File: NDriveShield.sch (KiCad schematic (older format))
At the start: 47 parts, among them J1 M03, J2 M03, J3 M03, J4 M03, J5 M03, J6 M03, Q1 NTD5867NLT4G, Q2 NTD5867NLT4G, Q3 NTD5867NLT4G, Q4 NTD5867NLT4G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

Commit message: Draft layout 1
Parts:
- removed J6: M03, symbol M03
- removed Q6: NTD5867NLT4G, symbol MOSFET_N
- removed RG6: 1K, symbol RES
- removed RG7: 10K, symbol RES
- removed SJD1, SJD2, SJD3, SJD4, SJD5, SJD6, SJG6, SJS6: SJ, symbol SJ
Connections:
- net labels removed: D11, DRAIN6, GATE6, SOURCE6, VCC, VIN
- wire segments 113 -> 95

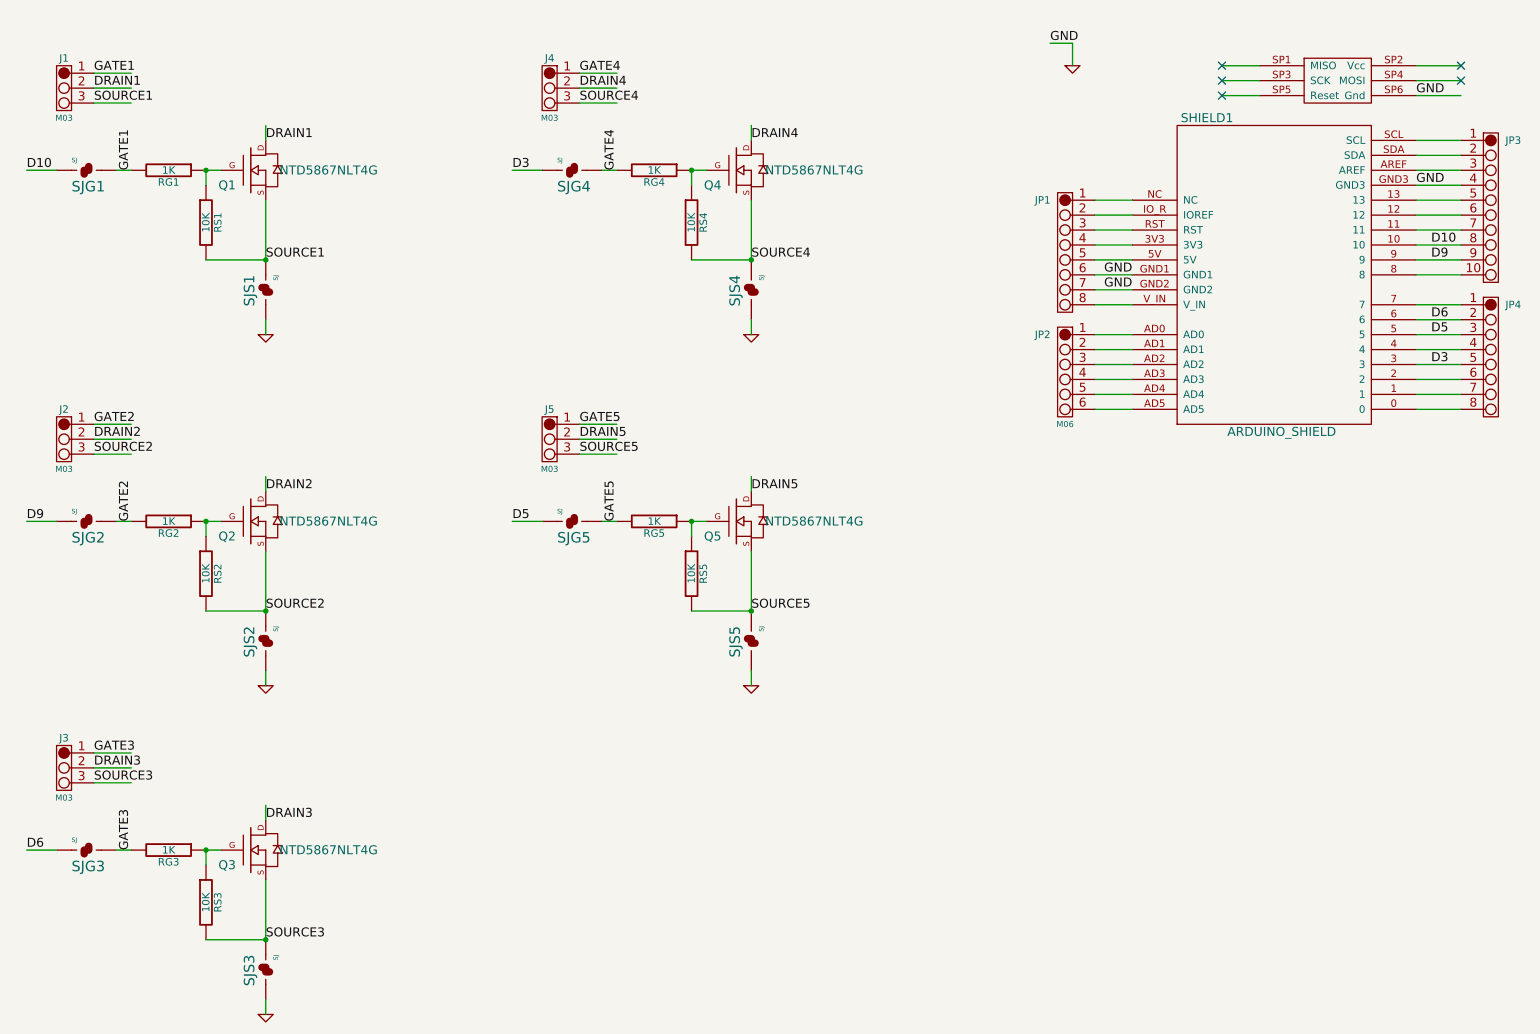
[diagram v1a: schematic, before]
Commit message: NDriveShield first prototype v0.1
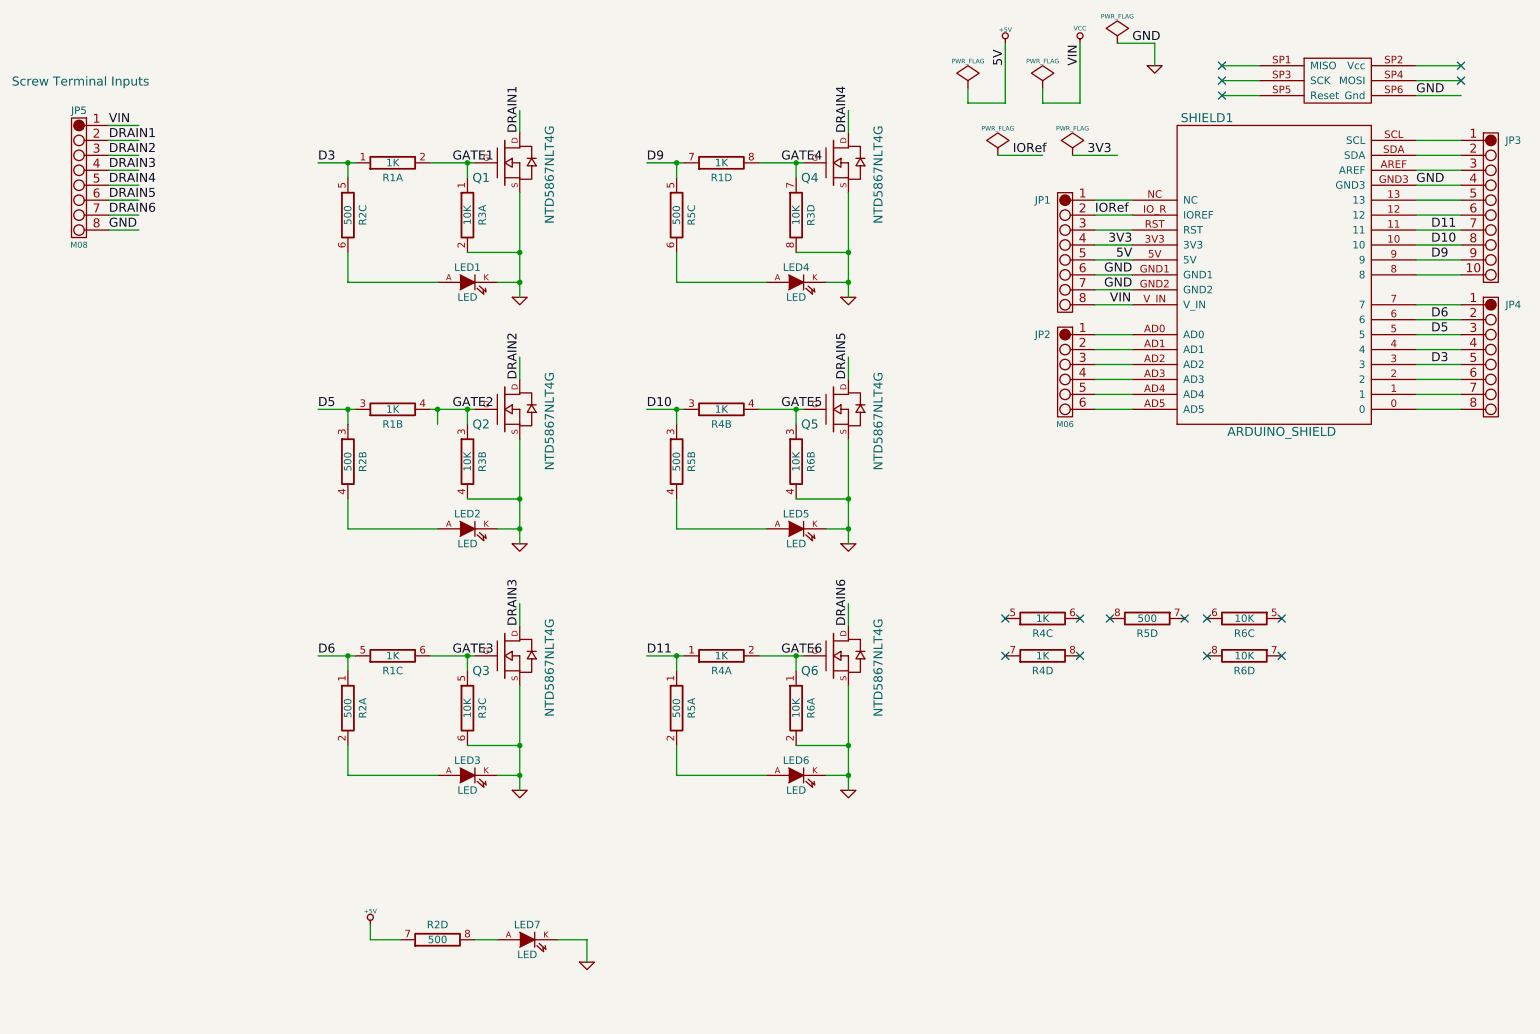
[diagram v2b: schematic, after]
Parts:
- removed J1, J2, J3, J4, J5: M03, symbol M03
- removed RG1, RG2, RG3, RG4, RG5: 1K, symbol RES
- removed RS1, RS2, RS3, RS4, RS5: 10K, symbol RES
- removed SJG1, SJG2, SJG3, SJG4, SJG5, SJS1, SJS2, SJS3, SJS4, SJS5: SJ, symbol SJ
- added JP5: M08, symbol M08
- added LED1, LED2, LED3, LED4, LED5, LED6, LED7: LED, symbol LED
- added Q6: NTD5867NLT4G, symbol MOSFET_N
- added R1, R4: 1K, symbol RES_PACK4_IND
- added R2, R5: 500, symbol RES_PACK4_IND
- added R3, R6: 10K, symbol RES_PACK4_IND
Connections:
- net labels added: +5V, 3V3, 5V, D11, DRAIN6, GATE6, IORef, VCC, VIN
- net labels removed: SOURCE1, SOURCE2, SOURCE3, SOURCE4, SOURCE5
- wire segments 95 -> 122
- no-connect marks 5 -> 15
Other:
- note added: "Screw Terminal Inputs\n"
- moved on the sheet: Q1

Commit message: Layout cleanup, fix EtherTen/Mega/Due jack clearance, update to V1.0
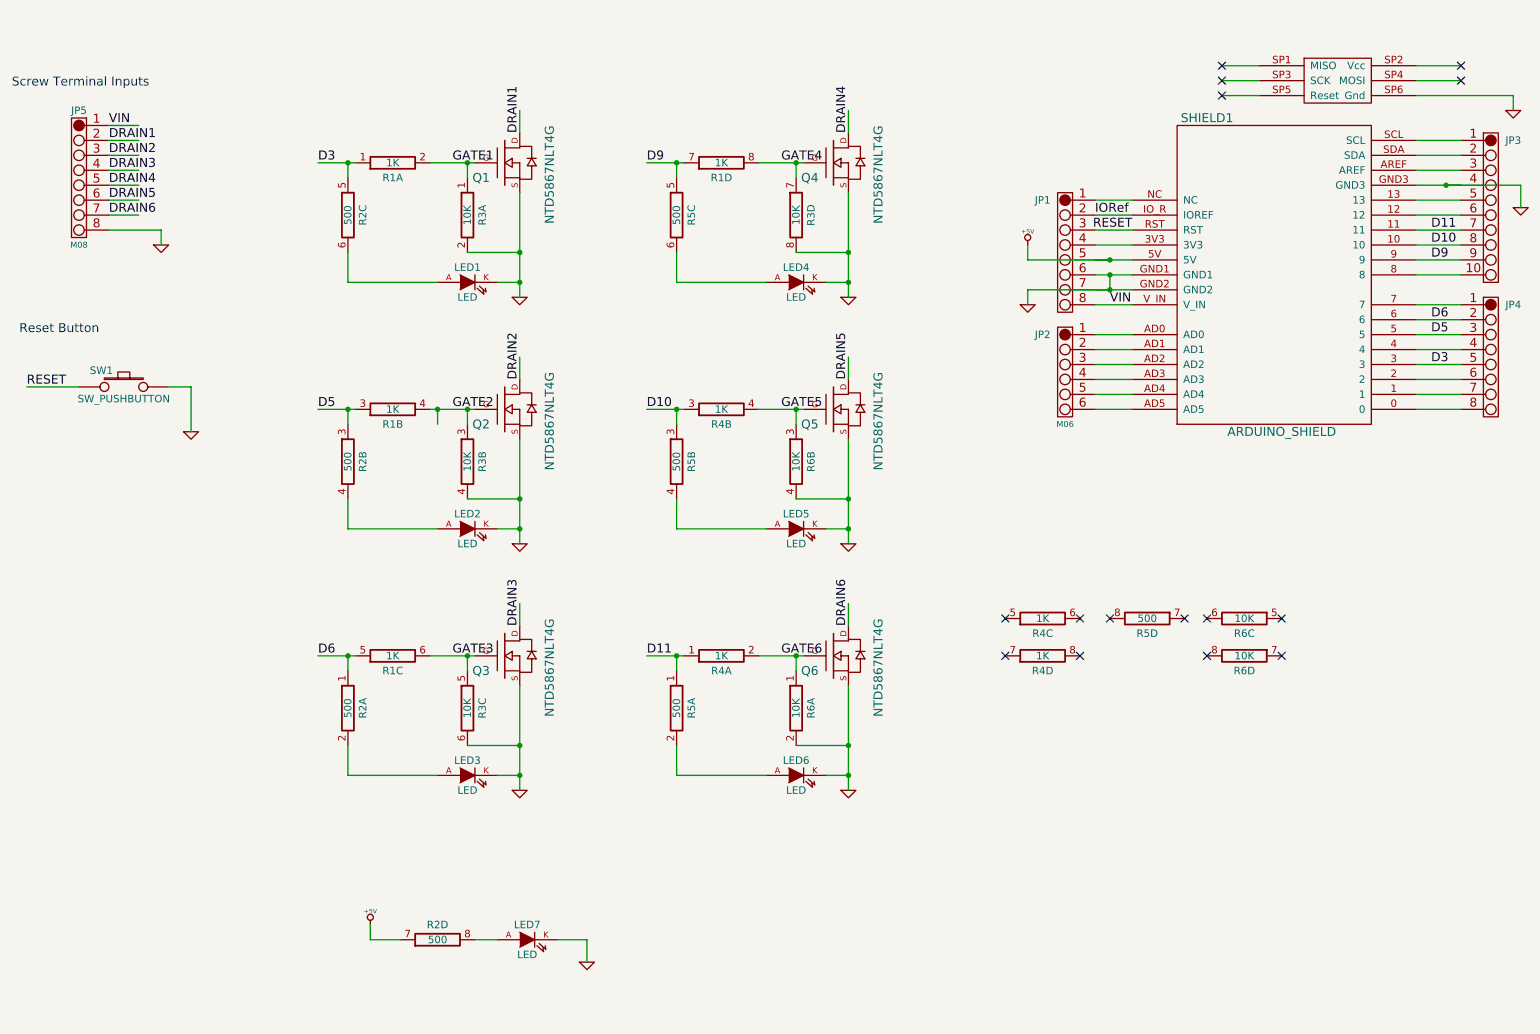
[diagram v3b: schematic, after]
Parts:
- added SW1: SW_PUSHBUTTON, symbol SW_PUSHBUTTON
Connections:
- net labels added: RESET
- net labels removed: 3V3, 5V, VCC
- wire segments 122 -> 124
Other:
- note added: "Reset Button\n"

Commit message: Clean up exposed copper fill areas on bottom of board
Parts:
- R2, R5: value 500 -> 470R
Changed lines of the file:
@@
 LIBS:valves
 LIBS:NDriveShield-cache
-EELAYER 24 0
+EELAYER 25 0
 EELAYER END
 $Descr A4 11693 8268
@@
 P 3050 2150
 F 0 "R2" H 3050 2250 50  0000 C CNN
-F 1 "500" H 3050 2150 50  0000 C CNN
+F 1 "470R" H 3050 2150 50  0000 C CNN
 F 2 "" H 3050 2150 60  0000 C CNN
 F 3 "" H 3050 2150 60  0000 C CNN
@@
 P 3050 3800
 F 0 "R2" H 3050 3900 50  0000 C CNN
-F 1 "500" H 3050 3800 50  0000 C CNN
+F 1 "470R" H 3050 3800 50  0000 C CNN
 F 2 "" H 3050 3800 60  0000 C CNN
 F 3 "" H 3050 3800 60  0000 C CNN
@@
 P 5250 2150
 F 0 "R5" H 5250 2250 50  0000 C CNN
-F 1 "500" H 5250 2150 50  0000 C CNN
+F 1 "470R" H 5250 2150 50  0000 C CNN
 F 2 "" H 5250 2150 60  0000 C CNN
 F 3 "" H 5250 2150 60  0000 C CNN
@@
 P 5250 3800
 F 0 "R5" H 5250 3900 50  0000 C CNN
-F 1 "500" H 5250 3800 50  0000 C CNN
+F 1 "470R" H 5250 3800 50  0000 C CNN
 F 2 "" H 5250 3800 60  0000 C CNN
 F 3 "" H 5250 3800 60  0000 C CNN
@@
 P 3050 5450
 F 0 "R2" H 3050 5550 50  0000 C CNN
-F 1 "500" H 3050 5450 50  0000 C CNN
+F 1 "470R" H 3050 5450 50  0000 C CNN
 F 2 "" H 3050 5450 60  0000 C CNN
 F 3 "" H 3050 5450 60  0000 C CNN
@@
 P 5250 5450
 F 0 "R5" H 5250 5550 50  0000 C CNN
-F 1 "500" H 5250 5450 50  0000 C CNN
+F 1 "470R" H 5250 5450 50  0000 C CNN
 F 2 "" H 5250 5450 60  0000 C CNN
 F 3 "" H 5250 5450 60  0000 C CNN
@@
 P 3650 7000
 F 0 "R2" H 3650 7100 50  0000 C CNN
-F 1 "500" H 3650 7000 50  0000 C CNN
+F 1 "470R" H 3650 7000 50  0000 C CNN
 F 2 "" H 3650 7000 60  0000 C CNN
 F 3 "" H 3650 7000 60  0000 C CNN
@@
 P 8400 4850
 F 0 "R5" H 8400 4950 50  0000 C CNN
-F 1 "500" H 8400 4850 50  0000 C CNN
+F 1 "470R" H 8400 4850 50  0000 C CNN
 F 2 "" H 8400 4850 60  0000 C CNN
 F 3 "" H 8400 4850 60  0000 C CNN
